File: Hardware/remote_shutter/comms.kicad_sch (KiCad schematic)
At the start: 1 part

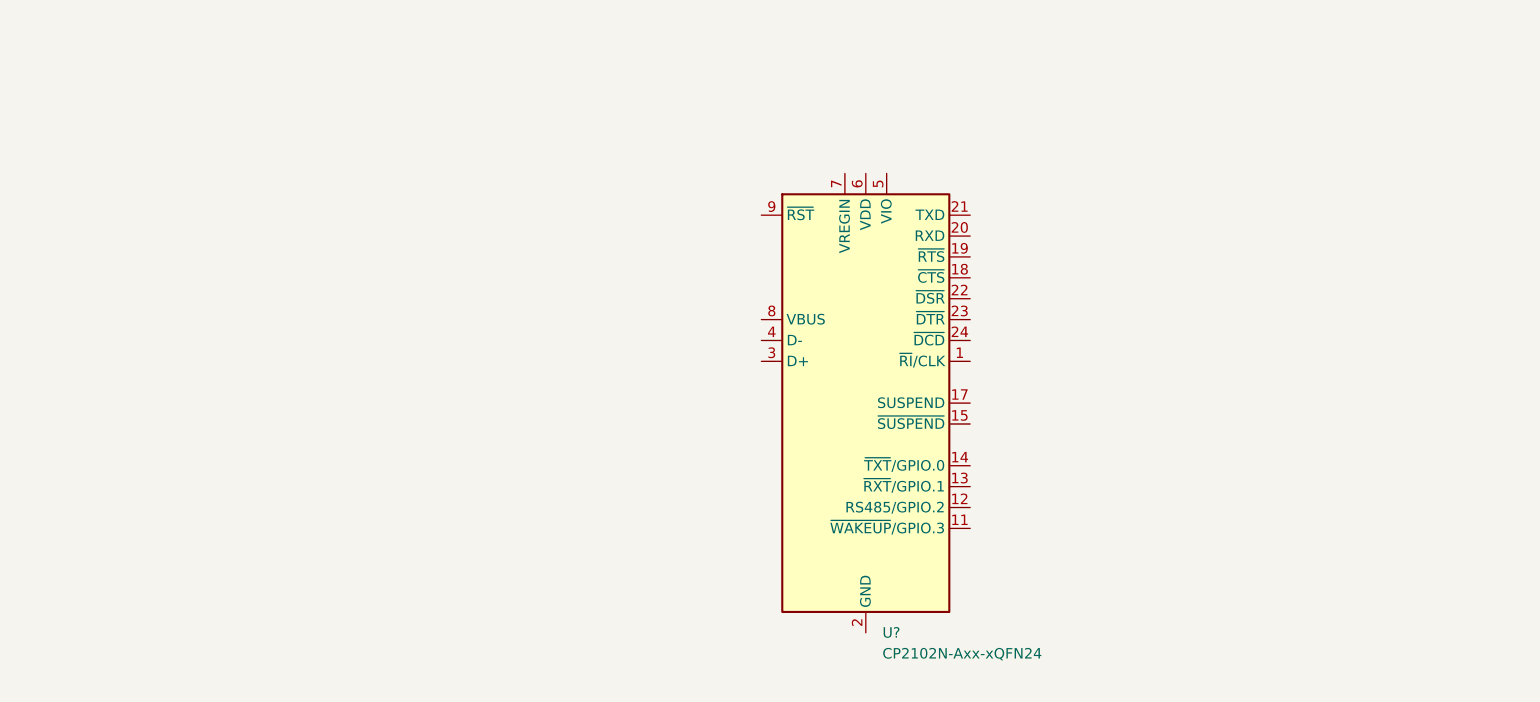
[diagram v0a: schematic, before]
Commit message: Added power & comms.
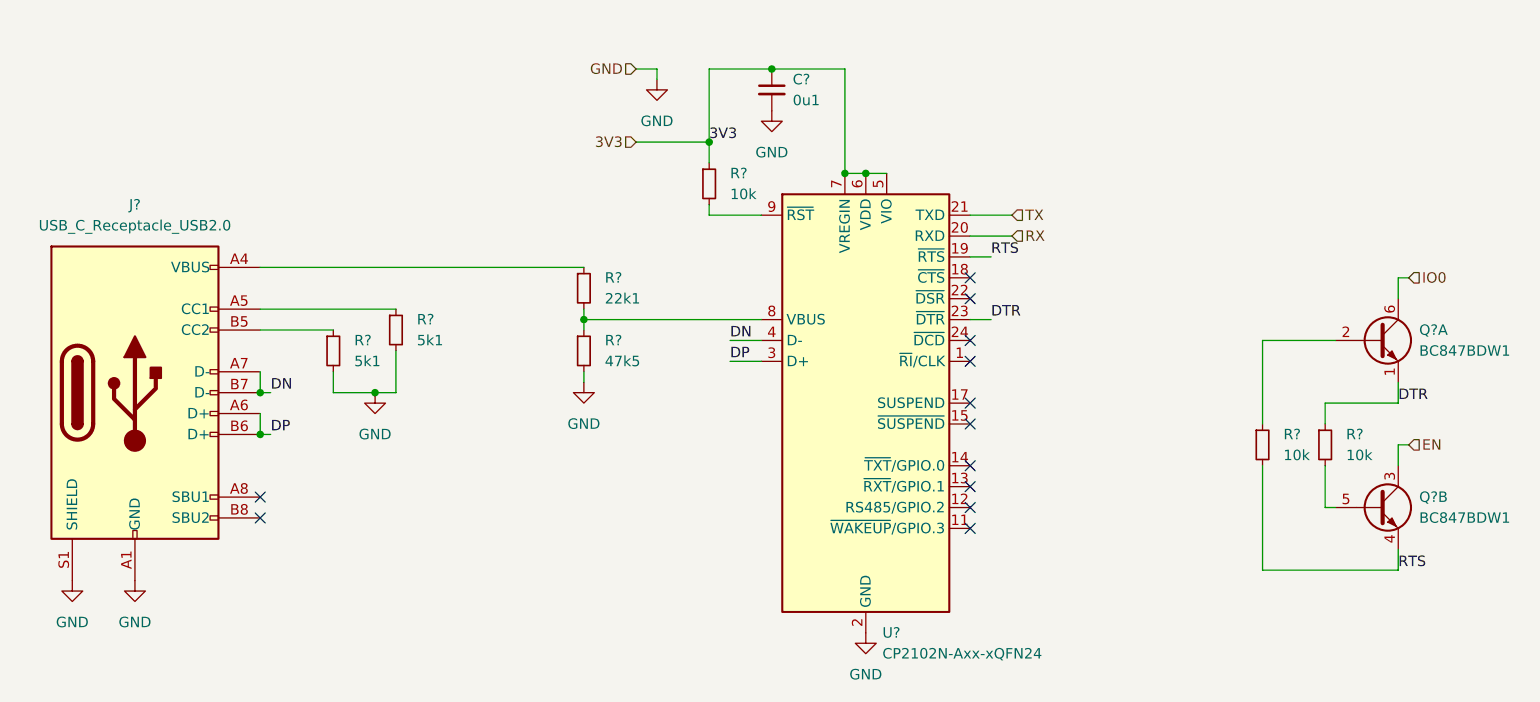
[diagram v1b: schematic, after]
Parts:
- added C?: 0u1, symbol Device:C_Small
- added J?: USB_C_Receptacle_USB2.0, symbol Connector:USB_C_Receptacle_USB2.0
- added Q? (x2): BC847BDW1, Package_TO_SOT_SMD:SOT-363_SC-70-6, symbol Transistor_BJT:BC847BDW1
- added R?: 47k5, symbol Device:R_Small
- added R? (x3): 10k, symbol Device:R_Small
- added R?: 22k1, symbol Device:R_Small
- added R? (x2): 5k1, symbol Device:R_Small
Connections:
- net RTS: now reaches U?.19 (~{RTS})
- net RTS: now also Q?.4 (E2), R?.2
- net GND: now reaches U?.2 (GND), U?.25 (GND)
- net GND: now also C?.2, J?.A1 (GND), J?.A12 (GND), J?.B1 (GND), J?.B12 (GND), J?.S1 (SHIELD), R?.2, R?.2, R?.2
- net RX: now reaches U?.20 (RXD)
- net TX: now reaches U?.21 (TXD)
- net DTR: now reaches U?.23 (~{DTR})
- net DTR: now also Q?.1 (E1), R?.1
- net DP: now reaches U?.3 (D+)
- net DP: now also J?.A6 (D+), J?.B6 (D+)
- net DN: now reaches U?.4 (D-)
- net DN: now also J?.A7 (D-), J?.B7 (D-)
- net 3V3: now reaches U?.5 (VIO)
- net 3V3: now also U?.6 (VDD), U?.7 (VREGIN), C?.1, R?.1
- net at U?.8 (VBUS): now also R?.1, R?.2
- net at U?.9 (~{RST}): now also R?.2
- new net: Q?.2 (B1), R?.1
- new net: Q?.5 (B2), R?.2
- new net: J?.A4 (VBUS), J?.A9 (VBUS), J?.B4 (VBUS), J?.B9 (VBUS), R?.1
- new net: J?.A5 (CC1), R?.1
- new net: J?.B5 (CC2), R?.1
- new net EN: Q?.3 (C2)
- new net IO0: Q?.6 (C1)
- no-connect marks 0 -> 12

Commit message: Added missing footprints. First PCB export.
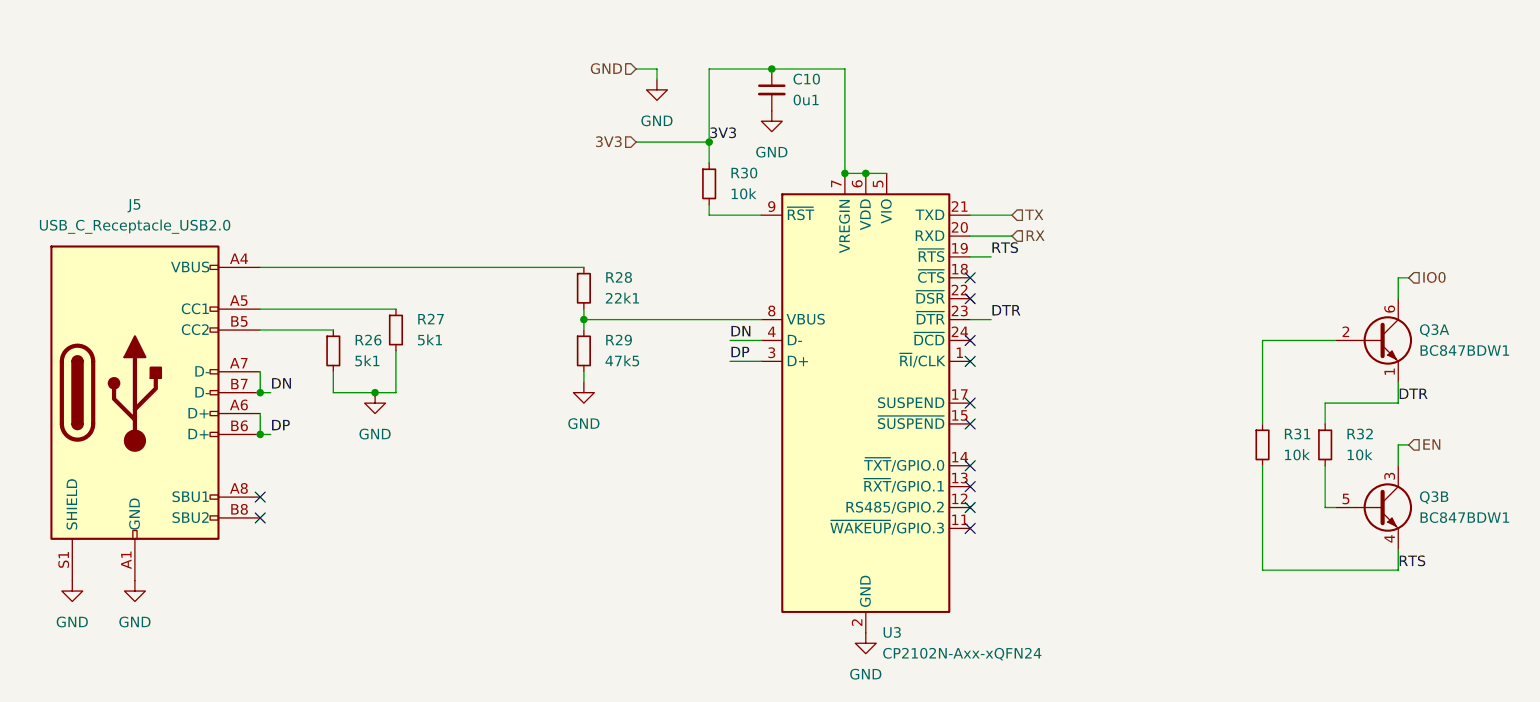
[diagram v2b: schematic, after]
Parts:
- C10: renamed from C?; footprint (none) -> Capacitor_SMD:C_0603_1608Metric_Pad1.08x0.95mm_HandSolder
- R26, R27, R28, R29, R30, R31, R32: renamed from R?; footprint (none) -> Resistor_SMD:R_0603_1608Metric_Pad0.98x0.95mm_HandSolder
- gave numbers to parts that had none: 3
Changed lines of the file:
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@@
   (symbol (lib_id "Interface_USB:CP2102N-Axx-xQFN24") (at 142.24 86.36 0) (unit 1)
     (in_bom yes) (on_board yes) (fields_autoplaced)
-    (property "Reference" "U?" (id 0) (at 144.2594 114.3 0)
+    (property "Reference" "U3" (id 0) (at 144.2594 114.3 0)
       (effects (font (size 1.27 1.27)) (justify left))
     )
@@
   (symbol (lib_id "power:GND") (at 130.81 50.8 0) (unit 1)
     (in_bom yes) (on_board yes) (fields_autoplaced)
-    (property "Reference" "#PWR?" (id 0) (at 130.81 57.15 0)
+    (property "Reference" "#PWR0118" (id 0) (at 130.81 57.15 0)
       (effects (font (size 1.27 1.27)) hide)
     )
@@
   (symbol (lib_id "Transistor_BJT:BC847BDW1") (at 204.47 78.74 0) (unit 1)
     (in_bom yes) (on_board yes) (fields_autoplaced)
-    (property "Reference" "Q?" (id 0) (at 209.55 77.4699 0)
+    (property "Reference" "Q3" (id 0) (at 209.55 77.4699 0)
       (effects (font (size 1.27 1.27)) (justify left))
     )
@@
   (symbol (lib_id "power:GND") (at 142.24 114.3 0) (unit 1)
     (in_bom yes) (on_board yes) (fields_autoplaced)
-    (property "Reference" "#PWR?" (id 0) (at 142.24 120.65 0)
+    (property "Reference" "#PWR0117" (id 0) (at 142.24 120.65 0)
       (effects (font (size 1.27 1.27)) hide)
     )
@@
   (symbol (lib_id "power:GND") (at 45.72 107.95 0) (unit 1)
     (in_bom yes) (on_board yes) (fields_autoplaced)
-    (property "Reference" "#PWR?" (id 0) (at 45.72 114.3 0)
+    (property "Reference" "#PWR0123" (id 0) (at 45.72 114.3 0)
       (effects (font (size 1.27 1.27)) hide)
     )
@@
   (symbol (lib_id "power:GND") (at 107.95 83.82 0) (unit 1)
     (in_bom yes) (on_board yes) (fields_autoplaced)
-    (property "Reference" "#PWR?" (id 0) (at 107.95 90.17 0)
+    (property "Reference" "#PWR0120" (id 0) (at 107.95 90.17 0)
       (effects (font (size 1.27 1.27)) hide)
     )
@@
   (symbol (lib_id "Device:R_Small") (at 107.95 80.01 0) (unit 1)
     (in_bom yes) (on_board yes) (fields_autoplaced)
-    (property "Reference" "R?" (id 0) (at 110.49 78.7399 0)
+    (property "Reference" "R29" (id 0) (at 110.49 78.7399 0)
       (effects (font (size 1.27 1.27)) (justify left))
     )
@@
       (effects (font (size 1.27 1.27)) (justify left))
     )
-    (property "Footprint" "" (id 2) (at 107.95 80.01 0)
+    (property "Footprint" "Resistor_SMD:R_0603_1608Metric_Pad0.98x0.95mm_HandSolder" (id 2) (at 107.95 80.01 0)
       (effects (font (size 1.27 1.27)) hide)
     )
@@
   (symbol (lib_id "Device:R_Small") (at 198.12 91.44 0) (unit 1)
     (in_bom yes) (on_board yes) (fields_autoplaced)
-    (property "Reference" "R?" (id 0) (at 200.66 90.1699 0)
+    (property "Reference" "R32" (id 0) (at 200.66 90.1699 0)
       (effects (font (size 1.27 1.27)) (justify left))
     )
@@
       (effects (font (size 1.27 1.27)) (justify left))
     )
-    (property "Footprint" "" (id 2) (at 198.12 91.44 0)
+    (property "Footprint" "Resistor_SMD:R_0603_1608Metric_Pad0.98x0.95mm_HandSolder" (id 2) (at 198.12 91.44 0)
       (effects (font (size 1.27 1.27)) hide)
     )
@@
   (symbol (lib_id "Device:R_Small") (at 107.95 72.39 0) (unit 1)
     (in_bom yes) (on_board yes) (fields_autoplaced)
-    (property "Reference" "R?" (id 0) (at 110.49 71.1199 0)
+    (property "Reference" "R28" (id 0) (at 110.49 71.1199 0)
       (effects (font (size 1.27 1.27)) (justify left))
     )
@@
       (effects (font (size 1.27 1.27)) (justify left))
     )
-    (property "Footprint" "" (id 2) (at 107.95 72.39 0)
+    (property "Footprint" "Resistor_SMD:R_0603_1608Metric_Pad0.98x0.95mm_HandSolder" (id 2) (at 107.95 72.39 0)
       (effects (font (size 1.27 1.27)) hide)
     )
@@
   (symbol (lib_id "Connector:USB_C_Receptacle_USB2.0") (at 53.34 85.09 0) (unit 1)
     (in_bom yes) (on_board yes) (fields_autoplaced)
-    (property "Reference" "J?" (id 0) (at 53.34 62.23 0))
+    (property "Reference" "J5" (id 0) (at 53.34 62.23 0))
     (property "Value" "USB_C_Receptacle_USB2.0" (id 1) (at 53.34 64.77 0))
     (property "Footprint" "" (id 2) (at 57.15 85.09 0)
@@
   (symbol (lib_id "power:GND") (at 116.84 46.99 0) (unit 1)
     (in_bom yes) (on_board yes) (fields_autoplaced)
-    (property "Reference" "#PWR?" (id 0) (at 116.84 53.34 0)
+    (property "Reference" "#PWR0119" (id 0) (at 116.84 53.34 0)
       (effects (font (size 1.27 1.27)) hide)
     )
@@
   (symbol (lib_id "Transistor_BJT:BC847BDW1") (at 204.47 99.06 0) (unit 2)
     (in_bom yes) (on_board yes) (fields_autoplaced)
-    (property "Reference" "Q?" (id 0) (at 209.55 97.7899 0)
+    (property "Reference" "Q3" (id 0) (at 209.55 97.7899 0)
       (effects (font (size 1.27 1.27)) (justify left))
     )
@@
   (symbol (lib_id "Device:R_Small") (at 123.19 59.69 0) (unit 1)
     (in_bom yes) (on_board yes) (fields_autoplaced)
-    (property "Reference" "R?" (id 0) (at 125.73 58.4199 0)
+    (property "Reference" "R30" (id 0) (at 125.73 58.4199 0)
       (effects (font (size 1.27 1.27)) (justify left))
     )
@@
       (effects (font (size 1.27 1.27)) (justify left))
     )
-    (property "Footprint" "" (id 2) (at 123.19 59.69 0)
+    (property "Footprint" "Resistor_SMD:R_0603_1608Metric_Pad0.98x0.95mm_HandSolder" (id 2) (at 123.19 59.69 0)
       (effects (font (size 1.27 1.27)) hide)
     )
@@
   (symbol (lib_id "Device:C_Small") (at 130.81 48.26 0) (unit 1)
     (in_bom yes) (on_board yes) (fields_autoplaced)
-    (property "Reference" "C?" (id 0) (at 133.35 46.9962 0)
+    (property "Reference" "C10" (id 0) (at 133.35 46.9962 0)
       (effects (font (size 1.27 1.27)) (justify left))
     )
@@
       (effects (font (size 1.27 1.27)) (justify left))
     )
-    (property "Footprint" "" (id 2) (at 130.81 48.26 0)
+    (property "Footprint" "Capacitor_SMD:C_0603_1608Metric_Pad1.08x0.95mm_HandSolder" (id 2) (at 130.81 48.26 0)
       (effects (font (size 1.27 1.27)) hide)
     )
@@
   (symbol (lib_id "power:GND") (at 53.34 107.95 0) (unit 1)
     (in_bom yes) (on_board yes) (fields_autoplaced)
-    (property "Reference" "#PWR?" (id 0) (at 53.34 114.3 0)
+    (property "Reference" "#PWR0122" (id 0) (at 53.34 114.3 0)
       (effects (font (size 1.27 1.27)) hide)
     )
@@
   (symbol (lib_id "Device:R_Small") (at 85.09 77.47 0) (unit 1)
     (in_bom yes) (on_board yes) (fields_autoplaced)
-    (property "Reference" "R?" (id 0) (at 87.63 76.1999 0)
+    (property "Reference" "R27" (id 0) (at 87.63 76.1999 0)
       (effects (font (size 1.27 1.27)) (justify left))
     )
@@
       (effects (font (size 1.27 1.27)) (justify left))
     )
-    (property "Footprint" "" (id 2) (at 85.09 77.47 0)
+    (property "Footprint" "Resistor_SMD:R_0603_1608Metric_Pad0.98x0.95mm_HandSolder" (id 2) (at 85.09 77.47 0)
       (effects (font (size 1.27 1.27)) hide)
     )
@@
   (symbol (lib_id "Device:R_Small") (at 190.5 91.44 0) (unit 1)
     (in_bom yes) (on_board yes) (fields_autoplaced)
-    (property "Reference" "R?" (id 0) (at 193.04 90.1699 0)
+    (property "Reference" "R31" (id 0) (at 193.04 90.1699 0)
       (effects (font (size 1.27 1.27)) (justify left))
     )
@@
       (effects (font (size 1.27 1.27)) (justify left))
     )
-    (property "Footprint" "" (id 2) (at 190.5 91.44 0)
+    (property "Footprint" "Resistor_SMD:R_0603_1608Metric_Pad0.98x0.95mm_HandSolder" (id 2) (at 190.5 91.44 0)
       (effects (font (size 1.27 1.27)) hide)
     )
@@
   (symbol (lib_id "power:GND") (at 82.55 85.09 0) (unit 1)
     (in_bom yes) (on_board yes) (fields_autoplaced)
-    (property "Reference" "#PWR?" (id 0) (at 82.55 91.44 0)
+    (property "Reference" "#PWR0121" (id 0) (at 82.55 91.44 0)
       (effects (font (size 1.27 1.27)) hide)
     )
@@
   (symbol (lib_id "Device:R_Small") (at 77.47 80.01 0) (unit 1)
     (in_bom yes) (on_board yes) (fields_autoplaced)
-    (property "Reference" "R?" (id 0) (at 80.01 78.7399 0)
+    (property "Reference" "R26" (id 0) (at 80.01 78.7399 0)
       (effects (font (size 1.27 1.27)) (justify left))
     )
@@
       (effects (font (size 1.27 1.27)) (justify left))
     )
-    (property "Footprint" "" (id 2) (at 77.47 80.01 0)
-      (effects (font (size 1.27 1.27)) hide)
-    )
+    (property "Footprint" "Resistor_SMD:R_0603_1608Metric_Pad0.98x0.95mm_HandSolder" (id 2) (at 77.47 80.01 0)
+      (effects (font (size 1.27 1.27)) hide)
+    )

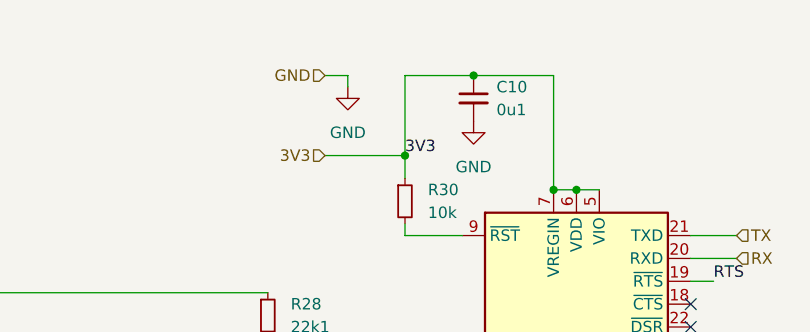
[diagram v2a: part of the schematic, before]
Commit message: Started routing. Added power switch.
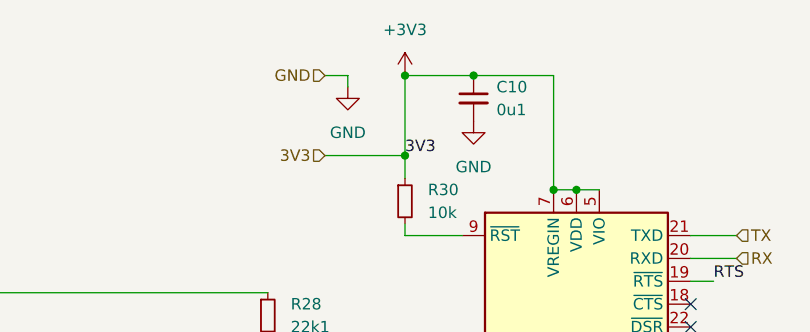
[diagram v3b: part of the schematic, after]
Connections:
- net 3V3 renamed +3V3
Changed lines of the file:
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@@
   (junction (at 68.58 85.09) (diameter 0) (color 0 0 0 0)
+  )
+  (junction (at 123.19 45.72) (diameter 0) (color 0 0 0 0)
   )
   (junction (at 107.95 76.2) (diameter 0) (color 0 0 0 0)
@@
       (effects (font (size 1.27 1.27)) hide)
     )
+    (pin "1")
+  )
+  (symbol (lib_id "power:+3V3") (at 123.19 45.72 0) (unit 1)
+    (in_bom yes) (on_board yes) (fields_autoplaced)
+    (property "Reference" "#PWR?" (id 0) (at 123.19 49.53 0)
+      (effects (font (size 1.27 1.27)) hide)
+    )
+    (property "Value" "+3V3" (id 1) (at 123.19 40.64 0))
+    (property "Footprint" "" (id 2) (at 123.19 45.72 0)
+      (effects (font (size 1.27 1.27)) hide)
+    )
+    (property "Datasheet" "" (id 3) (at 123.19 45.72 0)
+      (effects (font (size 1.27 1.27)) hide)
+    )
